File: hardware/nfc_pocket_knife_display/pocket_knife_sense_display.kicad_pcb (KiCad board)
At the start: 4 copper layers, 14.8 x 38.8 mm, 24 parts, among them U1 TMP117AIDRVR, U2 RF430CL330HIRGTR‎, U3 ATtiny1626-MFR

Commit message: preparation for e ink display via FPC
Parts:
- removed D2: CDBU0130L, Diode_SMD:D_0603_1608Metric
- added C1: 1 uF, Capacitor_SMD:C_0603_1608Metric, F.Cu at (164.6, 48.7)
- added J2: Conn_01x20_Pin, unsurv_offline_pcb_footprints:FH34SRJ-18S-0.5SH, B.Cu at (129.7, 66.5)
- added R3: 1k, Resistor_SMD:R_0603_1608Metric, F.Cu at (164.6, 51.2)
- added U4: ~, unsurv_offline_pcb_footprints:testpoint_array_2x3, F.Cu at (156.7, 49.0)
- C6: value 100uF -> 15 pF
- C7: value 1uf -> 8.3 pF
- D1: value CDBU0130L -> LED; footprint Diode_SMD:D_0603_1608Metric -> LED_SMD:LED_0603_1608Metric
- U2: value RF430CL330HIRGTR‎ -> NTAG link; footprint unsurv_offline_pcb_footprints:RF430_3x3mm_regular_noBCu -> unsurv_offline_pcb_footprints:NTAG 5 link
- moved U2 37.8 mm to (165.3, 44.3), turned to 0 degrees
- moved D1 36.1 mm to (164.7, 53.8), turned to 0 degrees
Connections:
- C3 pad 1: VCC -> VOUT
- C6 pad 1: VCC -> ANT2
- C6 pad 2: GND -> ANT1
- C7 pad 1: VCC -> ANT2
- C7 pad 2: GND -> ANT1
- C8 pad 1: VCC -> VOUT
- D1 pad 1: VCC -> GND
- D1 pad 2: ANT2 -> Net-(D1-A)
- R1 pad 1: VCC -> VOUT
- R2 pad 1: VCC -> VOUT
- TP4 pad 1: VCC -> VOUT
- U1 pad 5: VCC -> VOUT
- U2 pad 1: ANT1 -> GND
- U2 pad 10: SCL -> unconnected-(U2-HPD-Pad10)
- U2 pad 11: SDA -> GND
- U2 pad 12: Net-(U2-VCORE) -> VOUT
- U2 pad 13: GND -> unconnected-(U2-N.C-Pad13)
- U2 pad 14: unconnected-(U2-NC-Pad14) -> ANT2
- U2 pad 15: VCC -> ANT1
- U2 pad 2: ANT2 -> GND
- U2 pad 3: RF430_RST -> unconnected-(U2-N.C.-Pad3)
- U2 pad 4: GND -> unconnected-(U2-N.C.-Pad4)
- U2 pad 5: GND -> unconnected-(U2-N.C.-Pad5)
- U2 pad 6: GND -> SDA
- U2 pad 7: RF430_INT -> SCL
- U2 pad 8: GND -> ED
- U2 pad 9: GND -> VOUT
- U3 pad 4: VCC -> VOUT
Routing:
- net ANT2: track 9.50 -> 0.94 mm
- net ANT1: track 11.5 -> 3.71 mm
- net VCC: track 48.7 -> 44.9 mm, vias 7 -> 0
- net GND: track 61.2 -> 57.7 mm, vias 11 -> 10
- net RF430_RST: track 14.7 -> 13.1 mm, vias 2 -> 1
- net VOUT: vias 0 -> 7

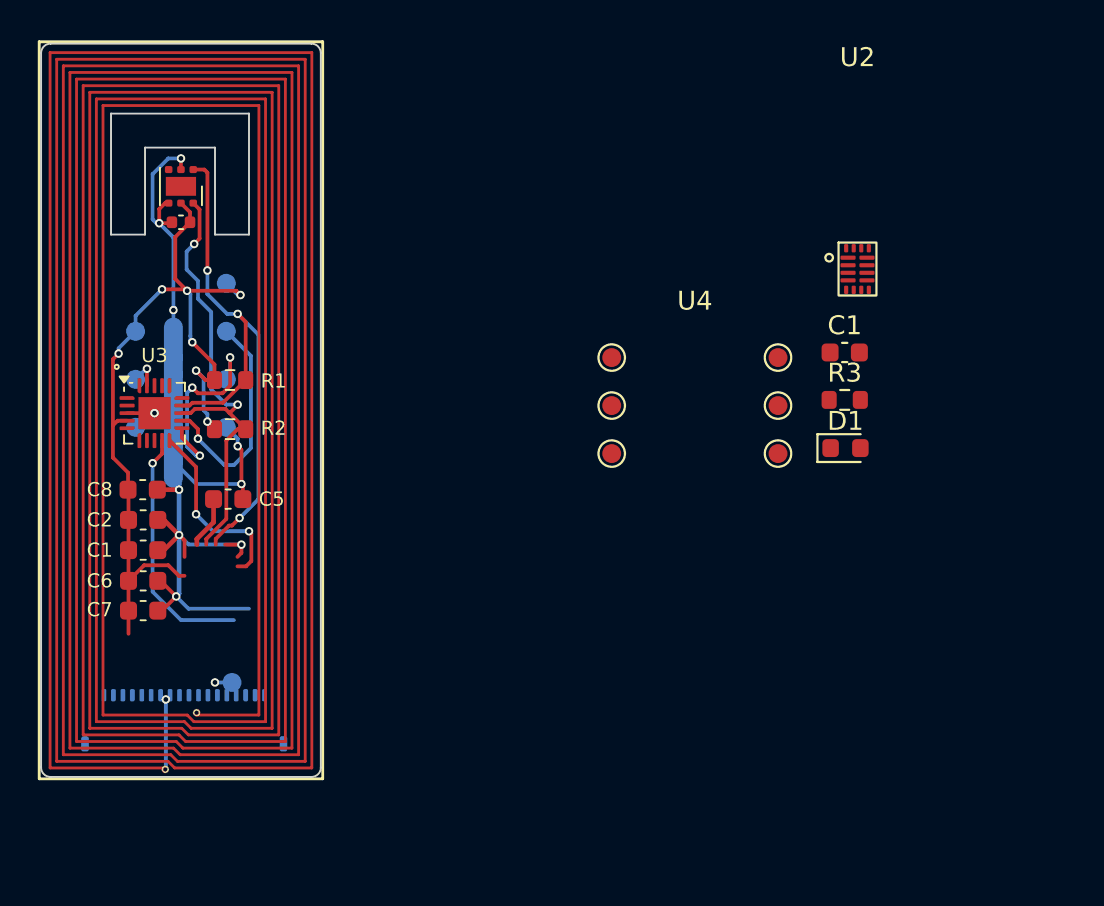
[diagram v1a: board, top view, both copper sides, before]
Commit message: add surface temperature version
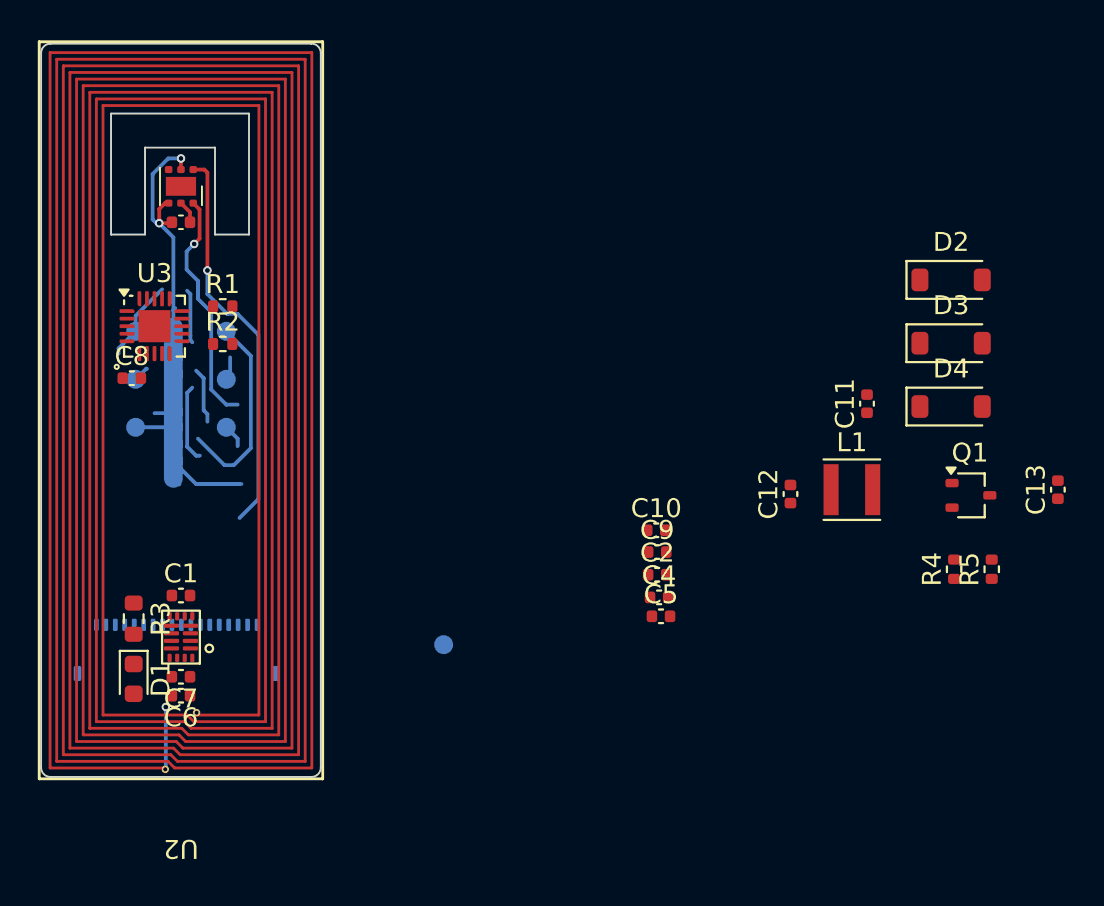
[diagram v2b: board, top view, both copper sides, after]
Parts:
- removed the C1 at (127.5, 59.2)
- removed the C1 at (164.6, 48.7)
- removed GND1, UPDI1, VCC1: TestPoint, TestPoint:TestPoint_Pad_D1.0mm
- removed U4: ~, unsurv_offline_pcb_footprints:testpoint_array_2x3
- added C1: 1 uF, Capacitor_SMD:C_0402_1005Metric, F.Cu at (129.5, 61.6)
- added C10: 1 uF 25 V, Capacitor_SMD:C_0402_1005Metric, F.Cu at (154.7, 58.1)
- added C11: 4.7uF, Capacitor_SMD:C_0402_1005Metric, F.Cu at (165.8, 51.5)
- added C12: 4.7uF, Capacitor_SMD:C_0402_1005Metric, F.Cu at (161.8, 56.2)
- added C13: 1uF, Capacitor_SMD:C_0402_1005Metric, F.Cu at (175.9, 56.0)
- added C4: 1 uF 25 V, Capacitor_SMD:C_0402_1005Metric, F.Cu at (154.8, 61.7)
- added C9: 1 uF 25 V, Capacitor_SMD:C_0402_1005Metric, F.Cu at (154.7, 59.3)
- added D2: MBR0530, Diode_SMD:D_SOD-123, F.Cu at (170.2, 44.9)
- added D3: MBR0530, Diode_SMD:D_SOD-123, F.Cu at (170.2, 48.2)
- added D4: MBR0530, Diode_SMD:D_SOD-123, F.Cu at (170.2, 51.6)
- added L1: 47uH 500mA, Inductor_SMD:L_Taiyo-Yuden_MD-3030, F.Cu at (165.0, 56.0)
- added Q1: Si1308EDL, Package_TO_SOT_SMD:SOT-323_SC-70, F.Cu at (171.3, 56.3)
- added R4: 2.2, Resistor_SMD:R_0402_1005Metric, F.Cu at (170.4, 60.2)
- added R5: 10k, Resistor_SMD:R_0402_1005Metric, F.Cu at (172.4, 60.2)
- added TP6: TestPoint, TestPoint:TestPoint_Pad_D1.0mm, B.Cu at (127.1, 50.2)
- added TP7: TestPoint, TestPoint:TestPoint_Pad_D1.0mm, B.Cu at (127.1, 52.7)
- C2: value 0.1 uF -> 1 uF 25 V; footprint Capacitor_SMD:C_0603_1608Metric -> Capacitor_SMD:C_0402_1005Metric
- C5: value 0.47 uF -> 1 uF 25 V; footprint Capacitor_SMD:C_0603_1608Metric -> Capacitor_SMD:C_0402_1005Metric
- C6, C7, C8: footprint Capacitor_SMD:C_0603_1608Metric -> Capacitor_SMD:C_0402_1005Metric
- R1, R2: footprint Resistor_SMD:R_0603_1608Metric -> Resistor_SMD:R_0402_1005Metric
- moved U2 40.8 mm to (129.5, 63.8), turned to 180 degrees
- moved D1 39.6 mm to (127.0, 66.0), turned to -90 degrees
- moved R3 39.4 mm to (127.0, 62.8), turned to -90 degrees
- moved C2 27.4 mm to (154.7, 60.5)
- moved C5 23.7 mm to (154.9, 62.7)
- moved TP5 11.4 mm to (143.4, 64.2)
- moved C6 6.40 mm to (129.5, 66.9), turned to 180 degrees
- moved C8 5.93 mm to (126.9, 50.1)
- moved TP4 5.43 mm to (127.1, 47.6)
- moved U3 4.60 mm to (128.1, 47.4)
- moved R2 4.53 mm to (131.7, 48.3)
- moved C7 4.03 mm to (129.5, 65.9), turned to 180 degrees
- moved R1 3.92 mm to (131.7, 46.3)
- moved J2 3.75 mm to (129.3, 62.8)
- moved QR_ref1 1.57 mm to (129.3, 57.1)
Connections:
- C2 pad 1: VCC -> GND
- C2 pad 2: GND -> Net-(J2-Pin_18)
- C3 pad 1: VOUT -> VCC
- C5 pad 1: Net-(U2-VCORE) -> GND
- C5 pad 2: GND -> Net-(J2-Pin_14)
- C8 pad 1: VOUT -> VCC
- J2 pad 1: unconnected-(J2-Pin_1-Pad1) -> GDR
- J2 pad 10: unconnected-(J2-Pin_10-Pad10) -> VCC
- J2 pad 11: unconnected-(J2-Pin_11-Pad11) -> GND
- J2 pad 12: unconnected-(J2-Pin_12-Pad12) -> Net-(J2-Pin_12)
- J2 pad 14: unconnected-(J2-Pin_14-Pad14) -> Net-(J2-Pin_14)
- J2 pad 15: unconnected-(J2-Pin_15-Pad15) -> PREVGH
- J2 pad 16: unconnected-(J2-Pin_16-Pad16) -> Net-(J2-Pin_16)
- J2 pad 17: unconnected-(J2-Pin_17-Pad17) -> PREVGL
- J2 pad 18: unconnected-(J2-Pin_18-Pad18) -> Net-(J2-Pin_18)
- J2 pad 19: unconnected-(J2-Pin_19-Pad19) -> GND
- J2 pad 2: unconnected-(J2-Pin_2-Pad2) -> RESE
- J2 pad 20: unconnected-(J2-Pin_20-Pad20) -> GND
- J2 pad 3: unconnected-(J2-Pin_3-Pad3) -> Net-(J2-Pin_3)
- J2 pad 4: unconnected-(J2-Pin_4-Pad4) -> BUSY
- J2 pad 5: unconnected-(J2-Pin_5-Pad5) -> RES
- J2 pad 6: unconnected-(J2-Pin_6-Pad6) -> D/C
- J2 pad 7: unconnected-(J2-Pin_7-Pad7) -> CS
- J2 pad 8: unconnected-(J2-Pin_8-Pad8) -> SCLK
- J2 pad 9: unconnected-(J2-Pin_9-Pad9) -> SDI
- R1 pad 1: VOUT -> VCC
- R2 pad 1: VOUT -> VCC
- R3 pad 1: VOUT -> VCC
- TP4 pad 1: VOUT -> VCC
- U1 pad 5: VOUT -> VCC
- U2 pad 12: VOUT -> VCC
- U2 pad 14: ANT2 -> ANT1
- U2 pad 15: ANT1 -> ANT2
- U2 pad 9: VOUT -> VCC
- U3 pad 4: VOUT -> VCC
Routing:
- net VCC: track 44.9 -> 11.5 mm
- net GND: track 57.7 -> 30.1 mm, vias 10 -> 2
- net RF430_RST: track 13.1 -> 0.00 mm, vias 1 -> 0
- net SDA: track 24.3 -> 12.6 mm, vias 2 -> 1
- net RF430_INT: track 10.1 -> 0.00 mm, vias 2 -> 0
- net SCL: track 30.6 -> 20.9 mm, vias 3 -> 1
- net RX: track 11.0 -> 5.35 mm, vias 3 -> 0
- net Net-(U2-VCORE): track 2.77 -> 0.00 mm
- net TX: track 12.0 -> 10.5 mm, vias 1 -> 0
- net UPDI: track 1.73 -> 0.83 mm, vias 1 -> 0
- net ANT2: track 0.94 -> 0.04 mm, vias 1 -> 0
- net VOUT: vias 7 -> 0
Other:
- board text added: "TX RX GND"
- board text added: "v 0.1 Made in Germany 11/25"
- board text removed: "VCC TX RX GND NFC"
- board text removed: "v 1.0 Made in Germany 04/25"
